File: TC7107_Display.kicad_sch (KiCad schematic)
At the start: 19 parts, among them IC1 TC7107ACPL, U3 TC7660SEPA, U4 ADR510ARTZ-REEL7

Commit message: Assigned Footprints to the components
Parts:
- IC1: footprint DIP1543W58P254L5175H635Q40N -> Package_DIP:DIP-40_W15.24mm
- U3: footprint PDIP8_300MC_MCH -> TC7660SEPA_footprints:PDIP8_300MC_MCH
- U4: footprint RT_3_ADI -> ul_ADR510ARTZ-REEL7_footprints:RT_3_ADI
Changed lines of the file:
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@@
 			)
 		)
-		(property "Footprint" "PDIP8_300MC_MCH"
+		(property "Footprint" "TC7660SEPA_footprints:PDIP8_300MC_MCH"
 			(at 35.56 29.21 0)
 			(hide yes)
@@
 			)
 		)
-		(property "Footprint" "DIP1543W58P254L5175H635Q40N"
+		(property "Footprint" "Package_DIP:DIP-40_W15.24mm"
 			(at 185.42 122.86 0)
 			(hide yes)
@@
 			)
 		)
-		(property "Footprint" "RT_3_ADI"
+		(property "Footprint" "ul_ADR510ARTZ-REEL7_footprints:RT_3_ADI"
 			(at 40.64 92.71 0)
 			(hide yes)

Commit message: Assigned more footprints on caps and resistors
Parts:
- C10, C11: footprint (none) -> Capacitor_SMD:C_1206_3216Metric_Pad1.33x1.80mm_HandSolder
- C12, C13, C17: footprint (none) -> Capacitor_SMD:C_0805_2012Metric_Pad1.18x1.45mm_HandSolder
- C14, C15: footprint (none) -> Capacitor_THT:C_Rect_L7.2mm_W2.5mm_P5.00mm_FKS2_FKP2_MKS2_MKP2
- C16: footprint (none) -> Capacitor_THT:C_Rect_L7.2mm_W7.2mm_P5.00mm_FKS2_FKP2_MKS2_MKP2
- R5, R6, R7, R8: footprint (none) -> Resistor_SMD:R_0805_2012Metric_Pad1.20x1.40mm_HandSolder
- RV1: footprint Resistor_THT:R_Array_SIP4 -> Potentiometer_THT:Potentiometer_Bourns_3296W_Vertical
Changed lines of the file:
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@@
 			)
 		)
-		(property "Footprint" ""
+		(property "Footprint" "Capacitor_SMD:C_0805_2012Metric_Pad1.18x1.45mm_HandSolder"
 			(at 104.14 30.1752 0)
 			(hide yes)
@@
 			)
 		)
-		(property "Footprint" ""
+		(property "Footprint" "Capacitor_SMD:C_0805_2012Metric_Pad1.18x1.45mm_HandSolder"
 			(at 137.16 28.9052 0)
 			(hide yes)
@@
 			)
 		)
-		(property "Footprint" ""
+		(property "Footprint" "Capacitor_SMD:C_1206_3216Metric_Pad1.33x1.80mm_HandSolder"
 			(at 20.6248 31.75 0)
 			(hide yes)
@@
 			)
 		)
-		(property "Footprint" ""
+		(property "Footprint" "Capacitor_SMD:C_1206_3216Metric_Pad1.33x1.80mm_HandSolder"
 			(at 110.1852 46.99 0)
 			(hide yes)
@@
 			)
 		)
-		(property "Footprint" ""
+		(property "Footprint" "Resistor_SMD:R_0805_2012Metric_Pad1.20x1.40mm_HandSolder"
 			(at 133.35 102.87 0)
 			(hide yes)
@@
 			)
 		)
-		(property "Footprint" ""
+		(property "Footprint" "Capacitor_SMD:C_0805_2012Metric_Pad1.18x1.45mm_HandSolder"
 			(at 196.85 105.7148 0)
 			(hide yes)
@@
 			)
 		)
-		(property "Footprint" ""
+		(property "Footprint" "Capacitor_THT:C_Rect_L7.2mm_W7.2mm_P5.00mm_FKS2_FKP2_MKS2_MKP2"
 			(at 147.0152 116.84 0)
 			(hide yes)
@@
 			)
 		)
-		(property "Footprint" ""
+		(property "Footprint" "Resistor_SMD:R_0805_2012Metric_Pad1.20x1.40mm_HandSolder"
 			(at 186.69 115.57 0)
 			(hide yes)
@@
 			)
 		)
-		(property "Footprint" ""
+		(property "Footprint" "Capacitor_THT:C_Rect_L7.2mm_W2.5mm_P5.00mm_FKS2_FKP2_MKS2_MKP2"
 			(at 207.9752 46.99 0)
 			(hide yes)
@@
 			)
 		)
-		(property "Footprint" ""
+		(property "Footprint" "Resistor_SMD:R_0805_2012Metric_Pad1.20x1.40mm_HandSolder"
 			(at 26.67 101.6 0)
 			(hide yes)
@@
 			)
 		)
-		(property "Footprint" ""
+		(property "Footprint" "Resistor_SMD:R_0805_2012Metric_Pad1.20x1.40mm_HandSolder"
 			(at 38.1 85.09 0)
 			(hide yes)
@@
 			)
 		)
-		(property "Footprint" ""
+		(property "Footprint" "Capacitor_THT:C_Rect_L7.2mm_W2.5mm_P5.00mm_FKS2_FKP2_MKS2_MKP2"
 			(at 122.8852 116.84 0)
 			(hide yes)
@@
 			)
 		)
-		(property "Footprint" "Resistor_THT:R_Array_SIP4"
+		(property "Footprint" "Potentiometer_THT:Potentiometer_Bourns_3296W_Vertical"
 			(at 38.1 74.93 0)
 			(hide yes)

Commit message: Update KiCad PCB
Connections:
- net VREF_1V: no longer R5.2, U4.1 (V+)
- new net: R5.2, U4.1 (V+)
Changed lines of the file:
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@@
-		)
-	)
-	(label "VREF_1V"
-		(at 34.29 105.41 270)
-		(effects
-			(font
-				(size 1.27 1.27)
-				(thickness 0.254)
-				(bold yes)
-			)
-			(justify right bottom)
 		)
 	)

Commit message: changed the footprint for C16 for the BOM
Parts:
- C16: footprint Capacitor_THT:C_Rect_L7.2mm_W7.2mm_P5.00mm_FKS2_FKP2_MKS2_MKP2 -> Capacitor_THT:C_Rect_L7.2mm_W3.0mm_P5.00mm_FKS2_FKP2_MKS2_MKP2
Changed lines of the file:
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@@
 			(justify left)
 		)
-		(property "Net Class" ""
+		(property "Netclass" ""
 			(at 200.66 52.07 0)
 			(show_name no)
@@
 			(justify left)
 		)
-		(property "Net Class" ""
+		(property "Netclass" ""
 			(at 200.66 54.61 0)
 			(show_name no)
@@
 			)
 		)
-		(property "Footprint" "Capacitor_THT:C_Rect_L7.2mm_W7.2mm_P5.00mm_FKS2_FKP2_MKS2_MKP2"
+		(property "Footprint" "Capacitor_THT:C_Rect_L7.2mm_W3.0mm_P5.00mm_FKS2_FKP2_MKS2_MKP2"
 			(at 147.0152 116.84 0)
 			(hide yes)

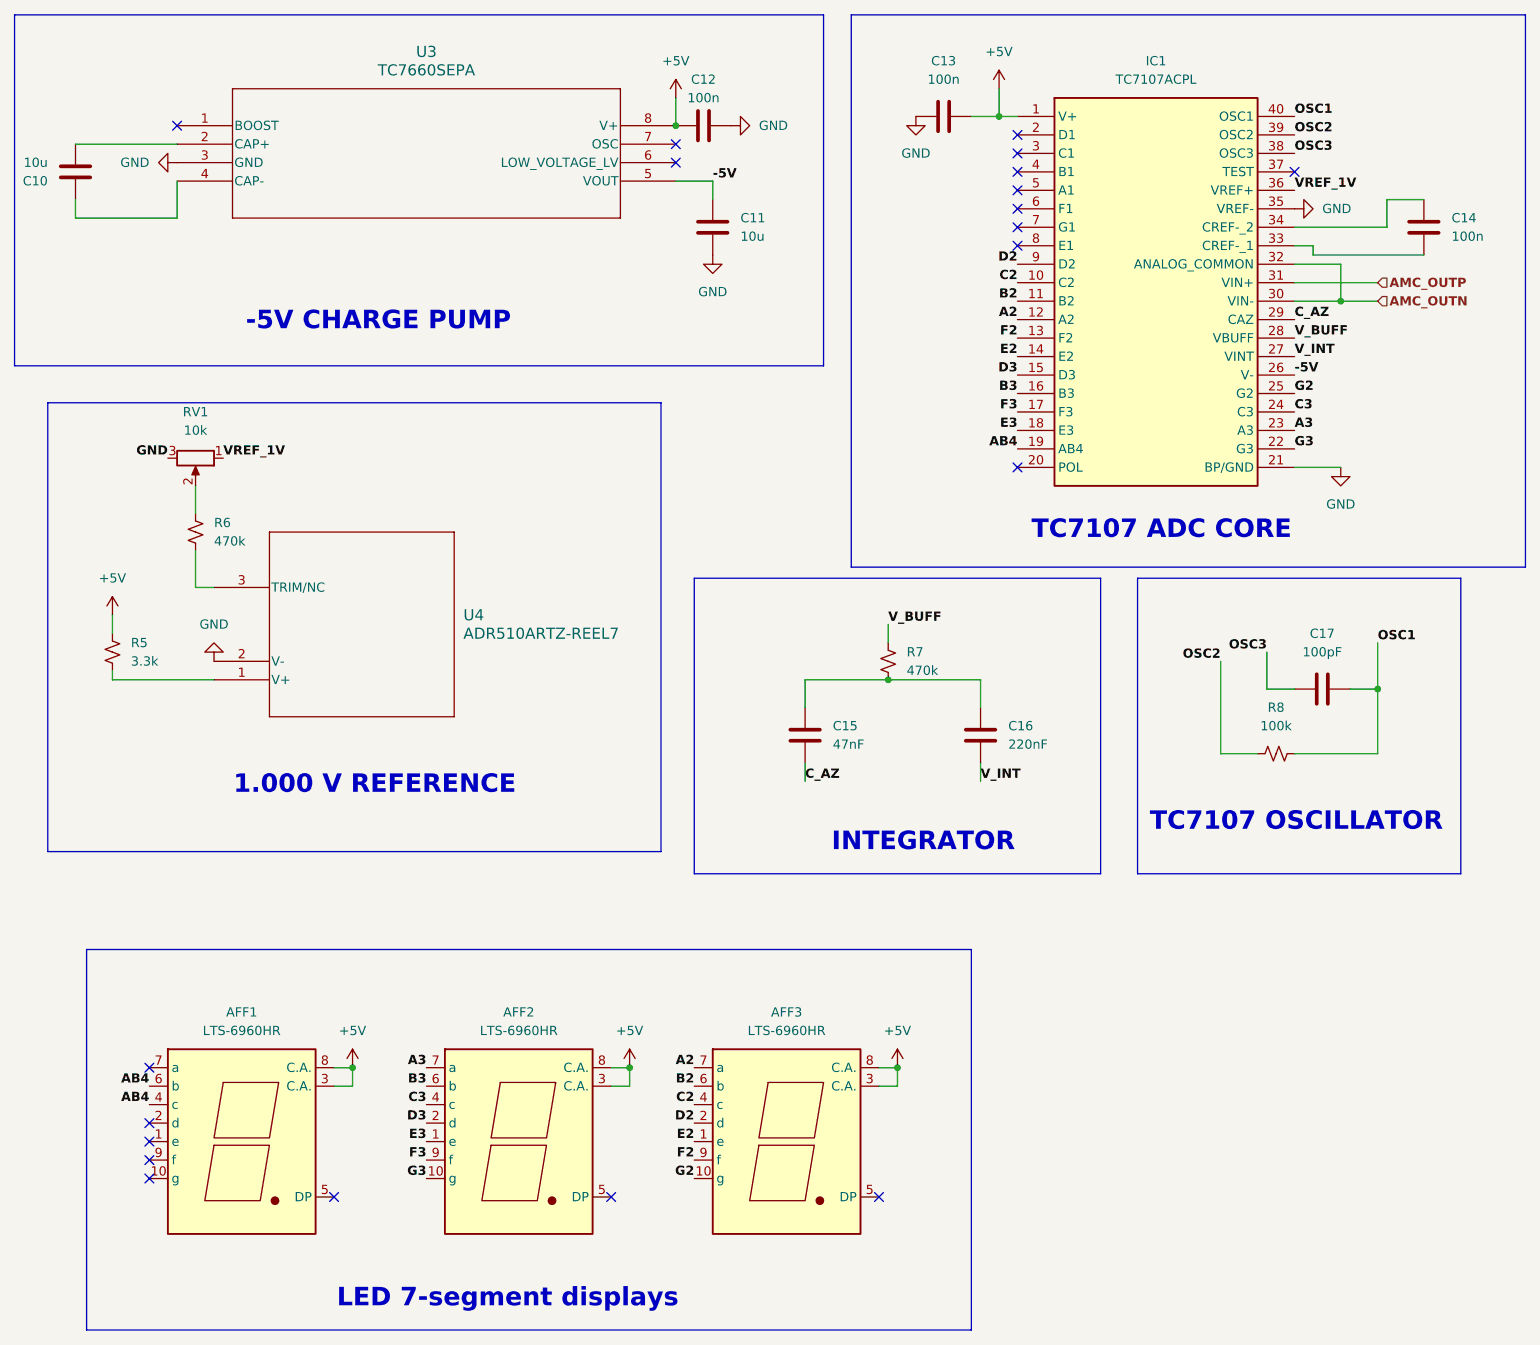
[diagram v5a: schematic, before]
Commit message: Replaced the AMC1311 and RECOME with AMC3311
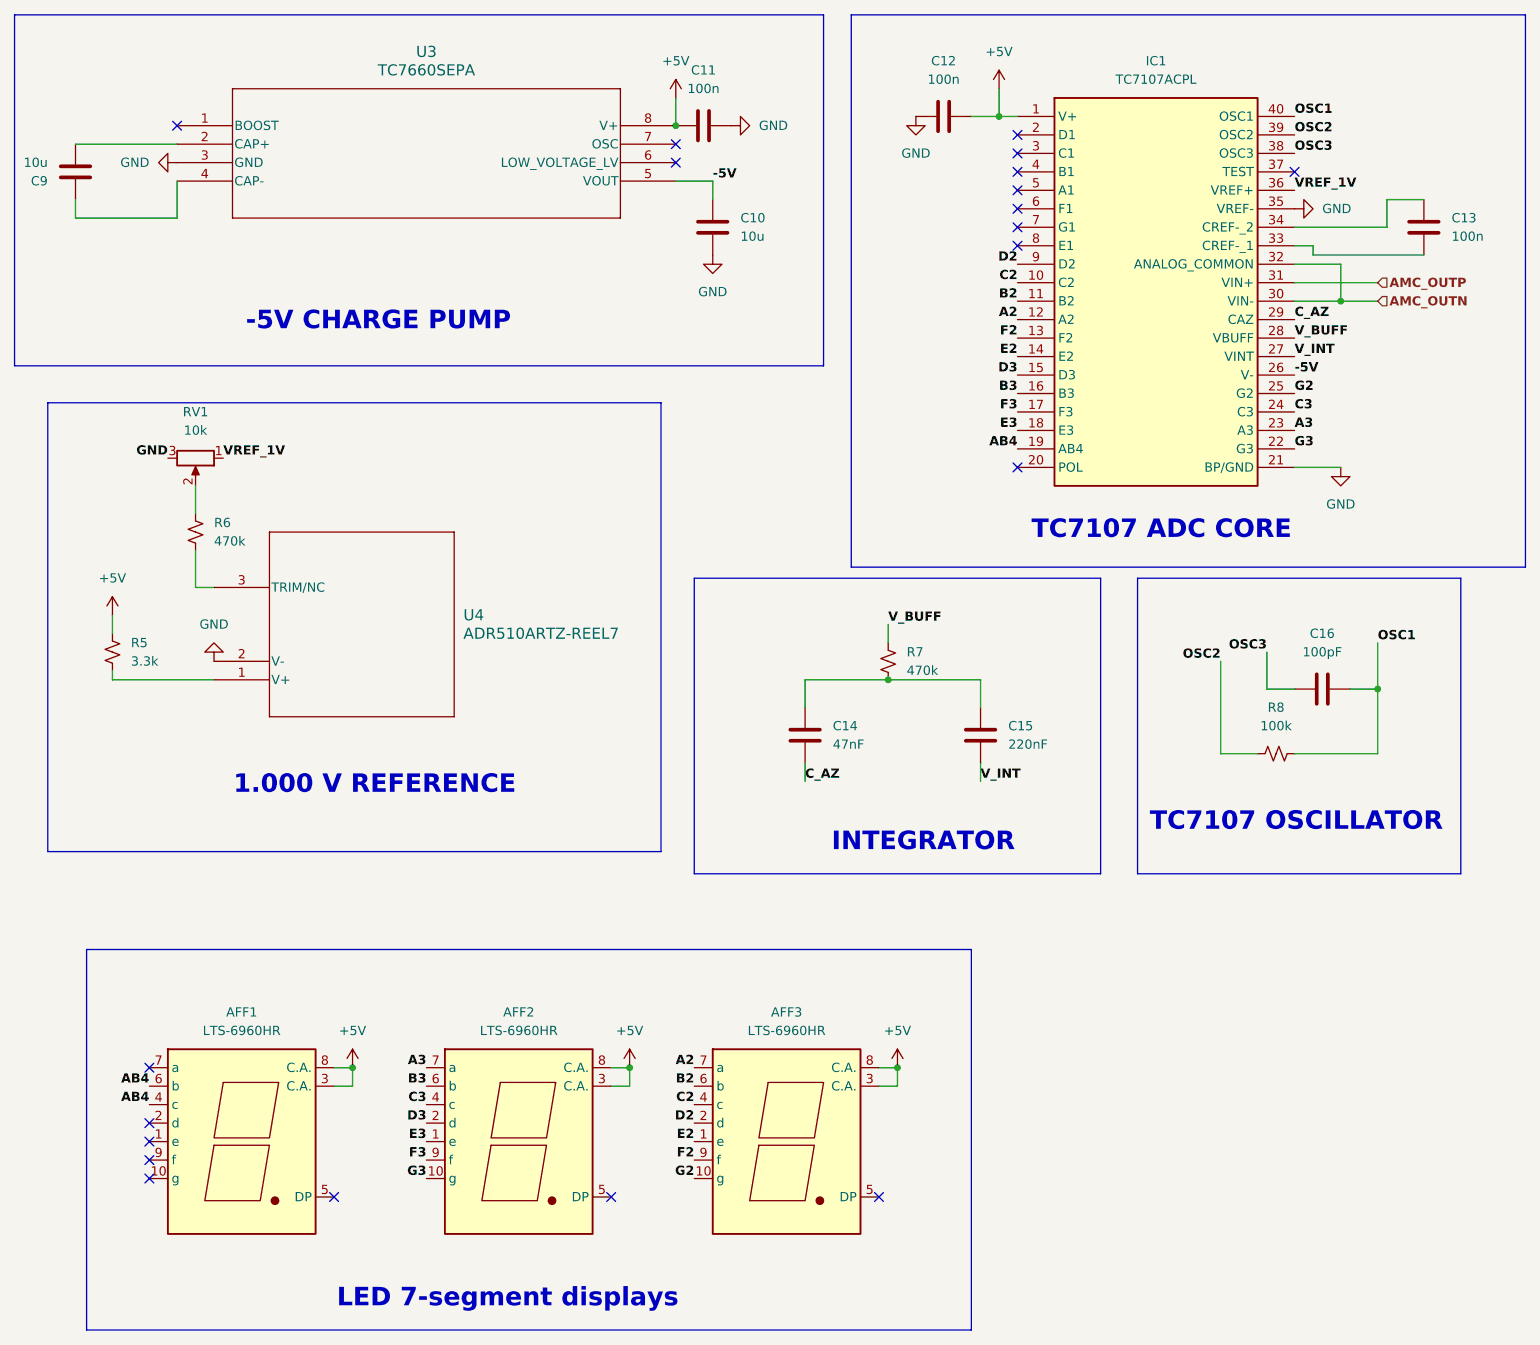
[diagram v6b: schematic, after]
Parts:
- renumbered C11 to C10, C12 to C11, C13 to C12, C14 to C13, C15 to C14, C16 to C15, C17 to C16, C10 to C9
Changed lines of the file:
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@@
 		(dnp no)
 		(fields_autoplaced yes)
-		(property "Reference" "C12"
-			(at 107.95 22.86 90)
+		(property "Reference" "C11"
+			(at 107.95 21.59 90)
 			(show_name no)
 			(do_not_autoplace no)
@@
 		)
 		(property "Value" "100n"
-			(at 107.95 25.4 90)
+			(at 107.95 24.13 90)
 			(show_name no)
 			(do_not_autoplace no)
@@
 			(project "Voltage-display"
 				(path "/aef1bf95-17d0-423a-9dc9-789356babb58/ee1a10b0-86e7-43a8-a51e-35d9aa7c3f38"
-					(reference "C12")
+					(reference "C11")
 					(unit 1)
 				)
@@
 		(dnp no)
 		(fields_autoplaced yes)
-		(property "Reference" "C13"
+		(property "Reference" "C12"
 			(at 140.97 20.32 90)
 			(show_name no)
@@
 			(project "Voltage-display"
 				(path "/aef1bf95-17d0-423a-9dc9-789356babb58/ee1a10b0-86e7-43a8-a51e-35d9aa7c3f38"
-					(reference "C13")
+					(reference "C12")
 					(unit 1)
 				)
@@
 		(in_pos_files yes)
 		(dnp no)
-		(property "Reference" "C10"
+		(property "Reference" "C9"
 			(at 17.78 36.8301 0)
 			(show_name no)
@@
 			(project "Voltage-display"
 				(path "/aef1bf95-17d0-423a-9dc9-789356babb58/ee1a10b0-86e7-43a8-a51e-35d9aa7c3f38"
-					(reference "C10")
+					(reference "C9")
 					(unit 1)
 				)
@@
 		(dnp no)
 		(fields_autoplaced yes)
-		(property "Reference" "C11"
+		(property "Reference" "C10"
 			(at 113.03 41.9099 0)
 			(show_name no)
@@
 			(project "Voltage-display"
 				(path "/aef1bf95-17d0-423a-9dc9-789356babb58/ee1a10b0-86e7-43a8-a51e-35d9aa7c3f38"
-					(reference "C11")
+					(reference "C10")
 					(unit 1)
 				)
@@
 		(dnp no)
 		(fields_autoplaced yes)
-		(property "Reference" "C17"
+		(property "Reference" "C16"
 			(at 193.04 99.06 90)
 			(show_name no)
@@
 			(project "Voltage-display"
 				(path "/aef1bf95-17d0-423a-9dc9-789356babb58/ee1a10b0-86e7-43a8-a51e-35d9aa7c3f38"
-					(reference "C17")
+					(reference "C16")
 					(unit 1)
 				)
@@
 		(dnp no)
 		(fields_autoplaced yes)
-		(property "Reference" "C16"
+		(property "Reference" "C15"
 			(at 149.86 111.7599 0)
 			(show_name no)
@@
 			(project "Voltage-display"
 				(path "/aef1bf95-17d0-423a-9dc9-789356babb58/ee1a10b0-86e7-43a8-a51e-35d9aa7c3f38"
-					(reference "C16")
+					(reference "C15")
 					(unit 1)
 				)
@@
 		(dnp no)
 		(fields_autoplaced yes)
-		(property "Reference" "C14"
+		(property "Reference" "C13"
 			(at 210.82 41.9099 0)
 			(show_name no)
@@
 			(project "Voltage-display"
 				(path "/aef1bf95-17d0-423a-9dc9-789356babb58/ee1a10b0-86e7-43a8-a51e-35d9aa7c3f38"
-					(reference "C14")
+					(reference "C13")
 					(unit 1)
 				)
@@
 		(dnp no)
 		(fields_autoplaced yes)
-		(property "Reference" "C15"
+		(property "Reference" "C14"
 			(at 125.73 111.7599 0)
 			(show_name no)
@@
 			(project "Voltage-display"
 				(path "/aef1bf95-17d0-423a-9dc9-789356babb58/ee1a10b0-86e7-43a8-a51e-35d9aa7c3f38"
-					(reference "C15")
-					(unit 1)
-				)
+					(reference "C14")
+					(unit 1)
+				)

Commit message: Silenced the erc
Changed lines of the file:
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@@
 	)
 	(junction
+		(at 104.14 21.59)
+		(diameter 0)
+		(color 0 0 0 0)
+	)
+	(junction
 		(at 133.35 105.41)
 		(diameter 0)
@@
 	(wire
 		(pts
-			(xy 104.14 25.4) (xy 104.14 29.21)
+			(xy 104.14 20.32) (xy 104.14 29.21)
 		)
 		(stroke
@@
 	(symbol
 		(lib_id "power:+5V")
-		(at 104.14 25.4 0)
+		(at 104.14 20.32 0)
 		(unit 1)
 		(body_style 1)
@@
 		(fields_autoplaced yes)
 		(property "Reference" "#PWR05"
-			(at 104.14 29.21 0)
+			(at 104.14 24.13 0)
 			(hide yes)
 			(show_name no)
@@
 		)
 		(property "Value" "+5V"
-			(at 104.14 20.32 0)
+			(at 104.14 15.24 0)
 			(show_name no)
 			(do_not_autoplace no)
@@
 		)
 		(property "Footprint" ""
-			(at 104.14 25.4 0)
+			(at 104.14 20.32 0)
 			(hide yes)
 			(show_name no)
@@
 		)
 		(property "Datasheet" ""
-			(at 104.14 25.4 0)
+			(at 104.14 20.32 0)
 			(hide yes)
 			(show_name no)
@@
 		)
 		(property "Description" "Power symbol creates a global label with name \"+5V\""
-			(at 104.14 25.4 0)
+			(at 104.14 20.32 0)
 			(hide yes)
 			(show_name no)
@@
 					(unit 1)
 				)
+			)
+		)
+	)
+	(symbol
+		(lib_id "power:PWR_FLAG")
+		(at 104.14 21.59 90)
+		(unit 1)
+		(body_style 1)
+		(exclude_from_sim no)
+		(in_bom yes)
+		(on_board yes)
+		(in_pos_files yes)
+		(dnp no)
+		(fields_autoplaced yes)
+		(property "Reference" "#FLG05"
+			(at 102.235 21.59 0)
+			(hide yes)
+			(show_name no)
+			(do_not_autoplace no)
+			(effects
+				(font
+					(size 1.27 1.27)
+				)
+			)
+		)
+		(property "Value" "PWR_FLAG"
+			(at 100.33 21.5899 90)
+			(show_name no)
+			(do_not_autoplace no)
+			(effects
+				(font
+					(size 1.27 1.27)
+				)
+				(justify left)
+			)
+		)
+		(property "Footprint" ""
+			(at 104.14 21.59 0)
+			(hide yes)
+			(show_name no)
+			(do_not_autoplace no)
+			(effects
+				(font
+					(size 1.27 1.27)
+				)
+			)
+		)
+		(property "Datasheet" ""
+			(at 104.14 21.59 0)
+			(hide yes)
+			(show_name no)
+			(do_not_autoplace no)
+			(effects
+				(font
+					(size 1.27 1.27)
+				)
+			)
+		)
+		(property "Description" "Special symbol for telling ERC where power comes from"
+			(at 104.14 21.59 0)
+			(hide yes)
+			(show_name no)
+			(do_not_autoplace no)
+			(effects
+				(font
+					(size 1.27 1.27)
+				)
+			)
+		)
+		(pin "1"
+		)
+		(instances
+			(project "Voltage-display"
+				(path "/aef1bf95-17d0-423a-9dc9-789356babb58/ee1a10b0-86e7-43a8-a51e-35d9aa7c3f38"
+					(reference "#FLG05")
+					(unit 1)
+				)

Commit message: Update schematic
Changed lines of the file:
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@@
 		(color 0 0 0 0)
 	)
+	(junction
+		(at 146.05 27.94)
+		(diameter 0)
+		(color 0 0 0 0)
+	)
 	(no_connect
 		(at 132.08 176.53)
@@
 	(wire
 		(pts
+			(xy 146.05 24.13) (xy 146.05 27.94)
+		)
+		(stroke
+			(width 0)
+			(type default)
+		)
+	)
+	(wire
+		(pts
 			(xy 200.66 106.68) (xy 200.66 115.57)
 		)
@@
 	(wire
 		(pts
+			(xy 146.05 27.94) (xy 148.59 27.94)
+		)
+		(stroke
+			(width 0)
+			(type default)
+		)
+	)
+	(wire
+		(pts
 			(xy 121.92 105.41) (xy 133.35 105.41)
 		)
@@
 	(wire
 		(pts
-			(xy 144.78 27.94) (xy 148.59 27.94)
+			(xy 144.78 27.94) (xy 146.05 27.94)
 		)
 		(stroke
@@
 			(justify left)
 		)
-		(property "Netclass" ""
+		(property "Net Class" ""
 			(at 200.66 52.07 0)
 			(show_name no)
@@
 			(justify left)
 		)
-		(property "Netclass" ""
+		(property "Net Class" ""
 			(at 200.66 54.61 0)
 			(show_name no)
@@
 		)
 	)
+	(hierarchical_label "+5V"
+		(shape input)
+		(at 146.05 24.13 90)
+		(effects
+			(font
+				(size 1.27 1.27)
+			)
+			(justify left)
+		)
+	)
 	(symbol
 		(lib_id "Device:C")
@@
 	)
 	(symbol
+		(lib_id "power:+5V")
+		(at 148.59 24.13 0)
+		(unit 1)
+		(body_style 1)
+		(exclude_from_sim no)
+		(in_bom yes)
+		(on_board yes)
+		(in_pos_files yes)
+		(dnp no)
+		(fields_autoplaced yes)
+		(property "Reference" "#PWR02"
+			(at 148.59 27.94 0)
+			(hide yes)
+			(show_name no)
+			(do_not_autoplace no)
+			(effects
+				(font
+					(size 1.27 1.27)
+				)
+			)
+		)
+		(property "Value" "+5V"
+			(at 148.59 19.05 0)
+			(show_name no)
+			(do_not_autoplace no)
+			(effects
+				(font
+					(size 1.27 1.27)
+				)
+			)
+		)
+		(property "Footprint" ""
+			(at 148.59 24.13 0)
+			(hide yes)
+			(show_name no)
+			(do_not_autoplace no)
+			(effects
+				(font
+					(size 1.27 1.27)
+				)
+			)
+		)
+		(property "Datasheet" ""
+			(at 148.59 24.13 0)
+			(hide yes)
+			(show_name no)
+			(do_not_autoplace no)
+			(effects
+				(font
+					(size 1.27 1.27)
+				)
+			)
+		)
+		(property "Description" "Power symbol creates a global label with name \"+5V\""
+			(at 148.59 24.13 0)
+			(hide yes)
+			(show_name no)
+			(do_not_autoplace no)
+			(effects
+				(font
+					(size 1.27 1.27)
+				)
+			)
+		)
+		(pin "1"
+		)
+		(instances
+			(project "Voltage-display"
+				(path "/aef1bf95-17d0-423a-9dc9-789356babb58/ee1a10b0-86e7-43a8-a51e-35d9aa7c3f38"
+					(reference "#PWR02")
+					(unit 1)
+				)
+			)
+		)
+	)
+	(symbol
 		(lib_id "Device:C")
 		(at 140.97 27.94 270)
@@
 					(unit 1)
 				)
-			)
-		)
-	)
-	(symbol
-		(lib_id "power:+5V")
-		(at 148.59 24.13 0)
-		(unit 1)
-		(body_style 1)
-		(exclude_from_sim no)
-		(in_bom yes)
-		(on_board yes)
-		(in_pos_files yes)
-		(dnp no)
-		(fields_autoplaced yes)
-		(property "Reference" "#PWR013"
-			(at 148.59 27.94 0)
-			(hide yes)
-			(show_name no)
-			(do_not_autoplace no)
-			(effects
-				(font
-					(size 1.27 1.27)
-				)
-			)
-		)
-		(property "Value" "+5V"
-			(at 148.59 19.05 0)
-			(show_name no)
-			(do_not_autoplace no)
-			(effects
-				(font
-					(size 1.27 1.27)
-				)
-			)
-		)
-		(property "Footprint" ""
-			(at 148.59 24.13 0)
-			(hide yes)
-			(show_name no)
-			(do_not_autoplace no)
-			(effects
-				(font
-					(size 1.27 1.27)
-				)
-			)
-		)
-		(property "Datasheet" ""
-			(at 148.59 24.13 0)
-			(hide yes)
-			(show_name no)
-			(do_not_autoplace no)
-			(effects
-				(font
-					(size 1.27 1.27)
-				)
-			)
-		)
-		(property "Description" "Power symbol creates a global label with name \"+5V\""
-			(at 148.59 24.13 0)
-			(hide yes)
-			(show_name no)
-			(do_not_autoplace no)
-			(effects
-				(font
-					(size 1.27 1.27)
-				)
-			)
-		)
-		(pin "1"
-		)
-		(instances
-			(project "Voltage-display"
-				(path "/aef1bf95-17d0-423a-9dc9-789356babb58/ee1a10b0-86e7-43a8-a51e-35d9aa7c3f38"
-					(reference "#PWR013")
-					(unit 1)
-				)
